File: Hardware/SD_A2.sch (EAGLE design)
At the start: 24 parts, among them IC1 74HCT245N, IC2 LM317, IC3 2716

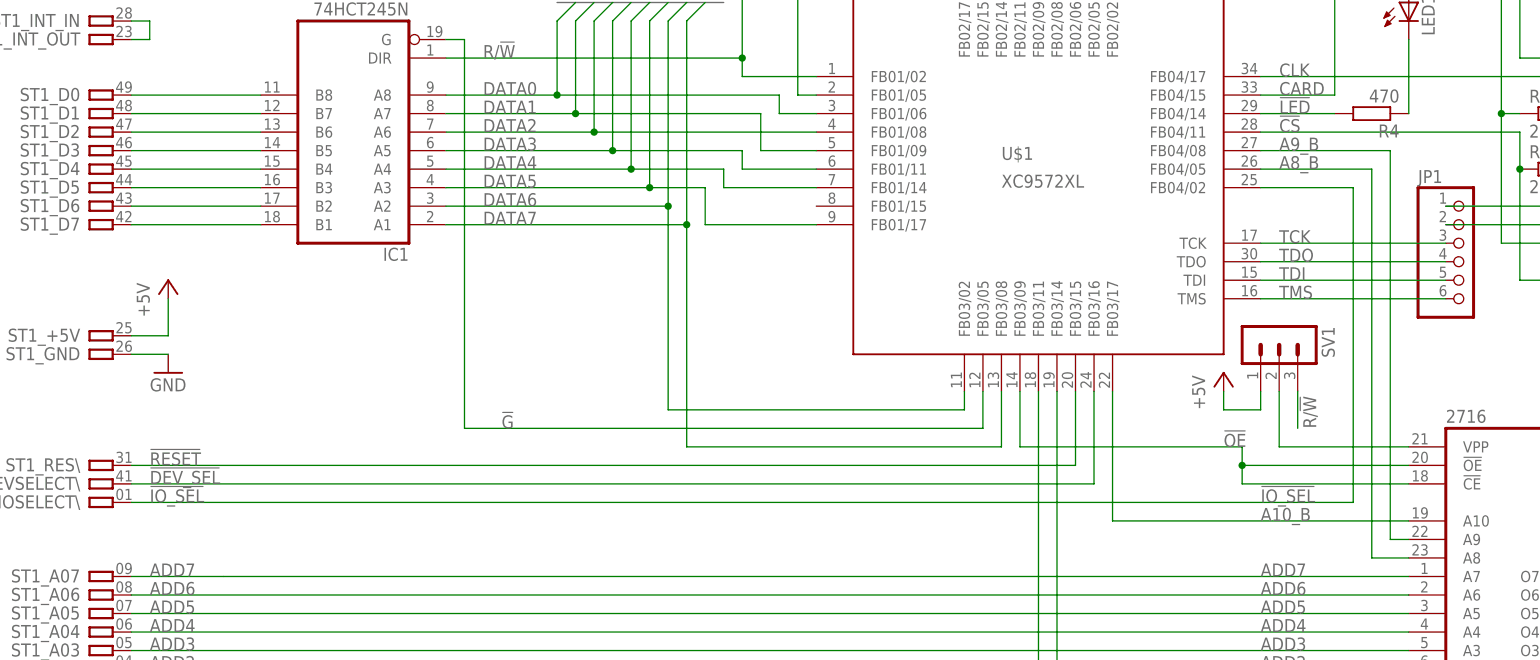
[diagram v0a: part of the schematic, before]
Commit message: Pinning changed
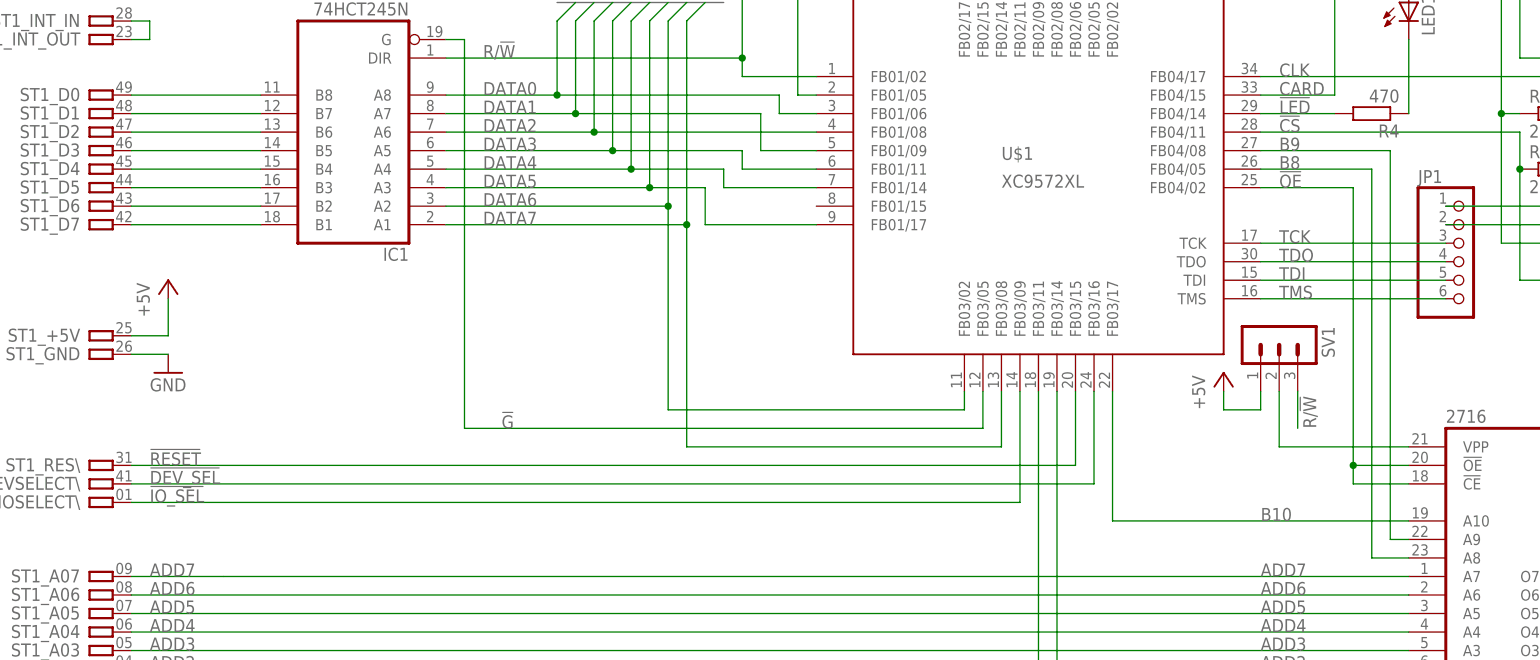
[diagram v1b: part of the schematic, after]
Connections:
- net A10_B renamed B10
- net A8_B renamed B8
- net A9_B renamed B9
- net !IO_SEL: now also U$1G$1.FB03/09; no longer U$1G$1.FB04/02
- net !OE: now also U$1G$1.FB04/02; no longer U$1G$1.FB03/09
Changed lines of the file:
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@@
 </segment>
 </net>
-<net name="A10_B" class="0">
+<net name="B10" class="0">
 <segment>
 <pinref part="IC3" gate="A" pin="A10"/>
@@
 </segment>
 </net>
-<net name="A9_B" class="0">
+<net name="B9" class="0">
 <segment>
 <pinref part="IC3" gate="A" pin="A9"/>
@@
 </segment>
 </net>
-<net name="A8_B" class="0">
+<net name="B8" class="0">
 <segment>
 <pinref part="IC3" gate="A" pin="A8"/>
@@
 <pinref part="U$1" gate="G$1" pin="FB04/05"/>
 <wire x1="246.38" y1="124.46" x2="231.14" y2="124.46" width="0.1524" layer="91"/>
-</segment>
-</net>
-<net name="!OE" class="0">
-<segment>
-<pinref part="U$1" gate="G$1" pin="FB03/09"/>
-<wire x1="198.12" y1="93.98" x2="198.12" y2="86.36" width="0.1524" layer="91"/>
-<wire x1="198.12" y1="86.36" x2="228.6" y2="86.36" width="0.1524" layer="91"/>
-<pinref part="IC3" gate="A" pin="!OE"/>
-<wire x1="251.46" y1="83.82" x2="228.6" y2="83.82" width="0.1524" layer="91"/>
-<wire x1="228.6" y1="83.82" x2="228.6" y2="86.36" width="0.1524" layer="91"/>
-<label x="226.06" y="86.36" size="1.778" layer="95"/>
-<pinref part="IC3" gate="A" pin="!CE"/>
-<wire x1="251.46" y1="81.28" x2="228.6" y2="81.28" width="0.1524" layer="91"/>
-<wire x1="228.6" y1="81.28" x2="228.6" y2="83.82" width="0.1524" layer="91"/>
-<junction x="228.6" y="83.82"/>
 </segment>
 </net>
@@
 </segment>
 </net>
-<net name="!IO_SEL" class="0">
-<segment>
-<label x="231.14" y="78.74" size="1.778" layer="95"/>
-<pinref part="U$1" gate="G$1" pin="FB04/02"/>
-<wire x1="231.14" y1="121.92" x2="243.84" y2="121.92" width="0.1524" layer="91"/>
-<wire x1="243.84" y1="121.92" x2="243.84" y2="78.74" width="0.1524" layer="91"/>
-<pinref part="ST1" gate="_IOSELECT\" pin="P"/>
-<wire x1="243.84" y1="78.74" x2="76.2" y2="78.74" width="0.1524" layer="91"/>
-<label x="78.74" y="78.74" size="1.778" layer="95"/>
-</segment>
-</net>
 <net name="!DEV_SEL" class="0">
 <segment>
@@
 </segment>
 </net>
+<net name="!OE" class="0">
+<segment>
+<label x="233.68" y="121.92" size="1.778" layer="95"/>
+<pinref part="U$1" gate="G$1" pin="FB04/02"/>
+<wire x1="231.14" y1="121.92" x2="243.84" y2="121.92" width="0.1524" layer="91"/>
+<pinref part="IC3" gate="A" pin="!OE"/>
+<wire x1="251.46" y1="83.82" x2="243.84" y2="83.82" width="0.1524" layer="91"/>
+<pinref part="IC3" gate="A" pin="!CE"/>
+<wire x1="251.46" y1="81.28" x2="243.84" y2="81.28" width="0.1524" layer="91"/>
+<wire x1="243.84" y1="81.28" x2="243.84" y2="83.82" width="0.1524" layer="91"/>
+<wire x1="243.84" y1="121.92" x2="243.84" y2="83.82" width="0.1524" layer="91"/>
+<junction x="243.84" y="83.82"/>
+</segment>
+</net>
+<net name="!IO_SEL" class="0">
+<segment>
+<pinref part="U$1" gate="G$1" pin="FB03/09"/>
+<wire x1="198.12" y1="93.98" x2="198.12" y2="78.74" width="0.1524" layer="91"/>
+<pinref part="ST1" gate="_IOSELECT\" pin="P"/>
+<wire x1="198.12" y1="78.74" x2="76.2" y2="78.74" width="0.1524" layer="91"/>
+<label x="78.74" y="78.74" size="1.778" layer="95"/>
+</segment>
+</net>

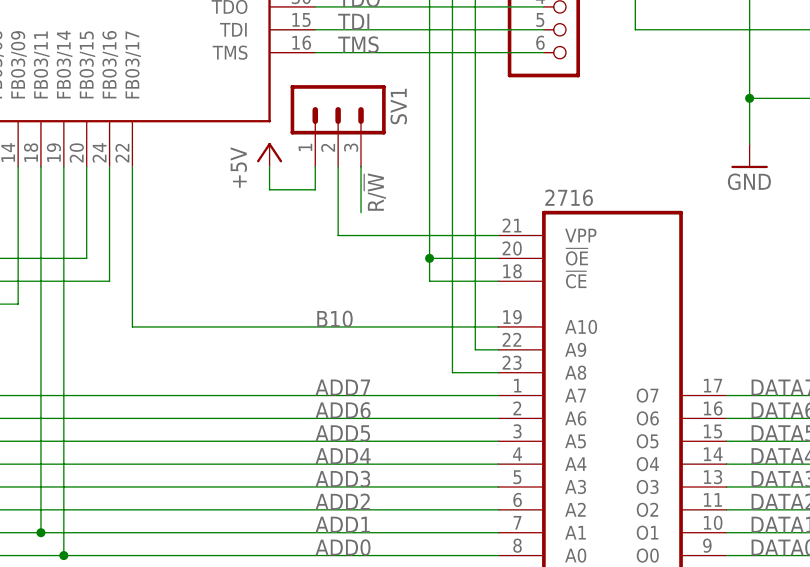
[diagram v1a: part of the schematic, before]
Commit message: !CE on GND
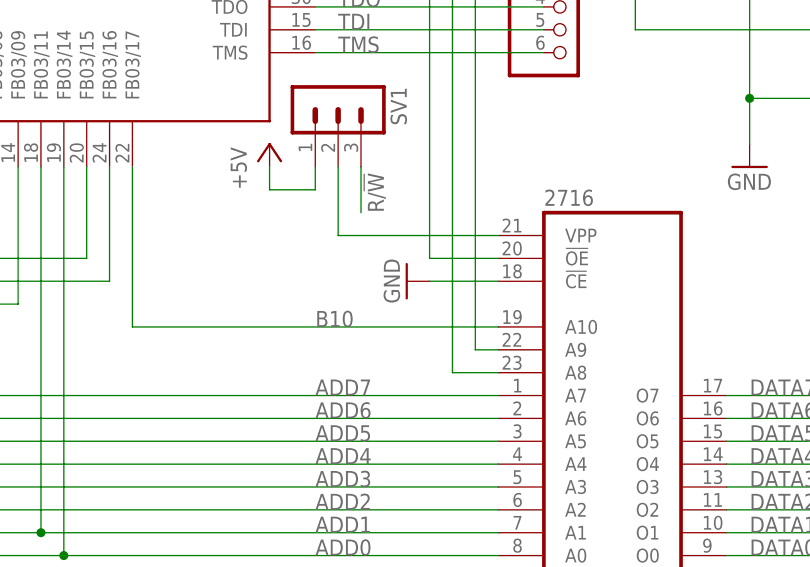
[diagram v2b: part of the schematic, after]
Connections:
- net !OE: no longer IC3A.!CE
- net GND: now also IC3A.!CE
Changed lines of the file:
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@@
 <part name="R10" library="rcl" library_urn="urn:adsk.eagle:library:334" deviceset="R-EU_" device="0204/7" value="10k"/>
 <part name="P+6" library="supply1" library_urn="urn:adsk.eagle:library:371" deviceset="+5V" device=""/>
+<part name="GND4" library="supply1" library_urn="urn:adsk.eagle:library:371" deviceset="GND" device=""/>
 </parts>
 <sheets>
@@
 <instance part="R10" gate="G$1" x="172.72" y="154.94"/>
 <instance part="P+6" gate="1" x="182.88" y="160.02"/>
+<instance part="GND4" gate="1" x="241.3" y="81.28" rot="R270"/>
 </instances>
 <busses>
@@
 <wire x1="256.54" y1="116.84" x2="279.4" y2="116.84" width="0.1524" layer="91"/>
 <junction x="279.4" y="116.84"/>
+</segment>
+<segment>
+<pinref part="IC3" gate="A" pin="!CE"/>
+<pinref part="GND4" gate="1" pin="GND"/>
+<wire x1="251.46" y1="81.28" x2="243.84" y2="81.28" width="0.1524" layer="91"/>
 </segment>
 </net>
@@
 <pinref part="IC3" gate="A" pin="!OE"/>
 <wire x1="251.46" y1="83.82" x2="243.84" y2="83.82" width="0.1524" layer="91"/>
-<pinref part="IC3" gate="A" pin="!CE"/>
-<wire x1="251.46" y1="81.28" x2="243.84" y2="81.28" width="0.1524" layer="91"/>
-<wire x1="243.84" y1="81.28" x2="243.84" y2="83.82" width="0.1524" layer="91"/>
 <wire x1="243.84" y1="121.92" x2="243.84" y2="83.82" width="0.1524" layer="91"/>
-<junction x="243.84" y="83.82"/>
-</segment>
-</net>
+</segment>
+</net>

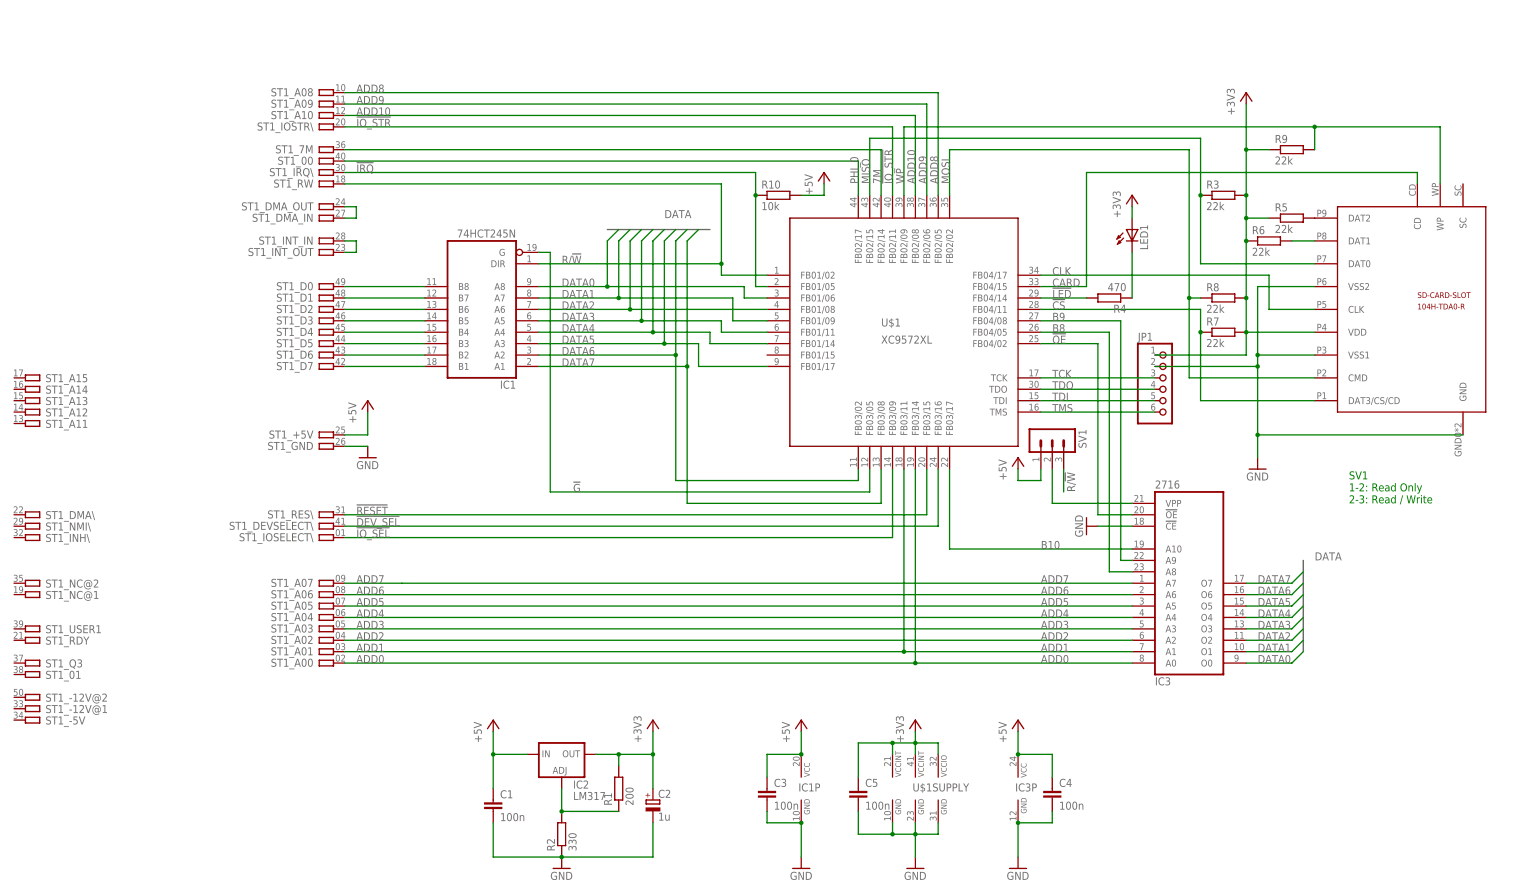
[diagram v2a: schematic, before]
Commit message: Pin changes, libraries added
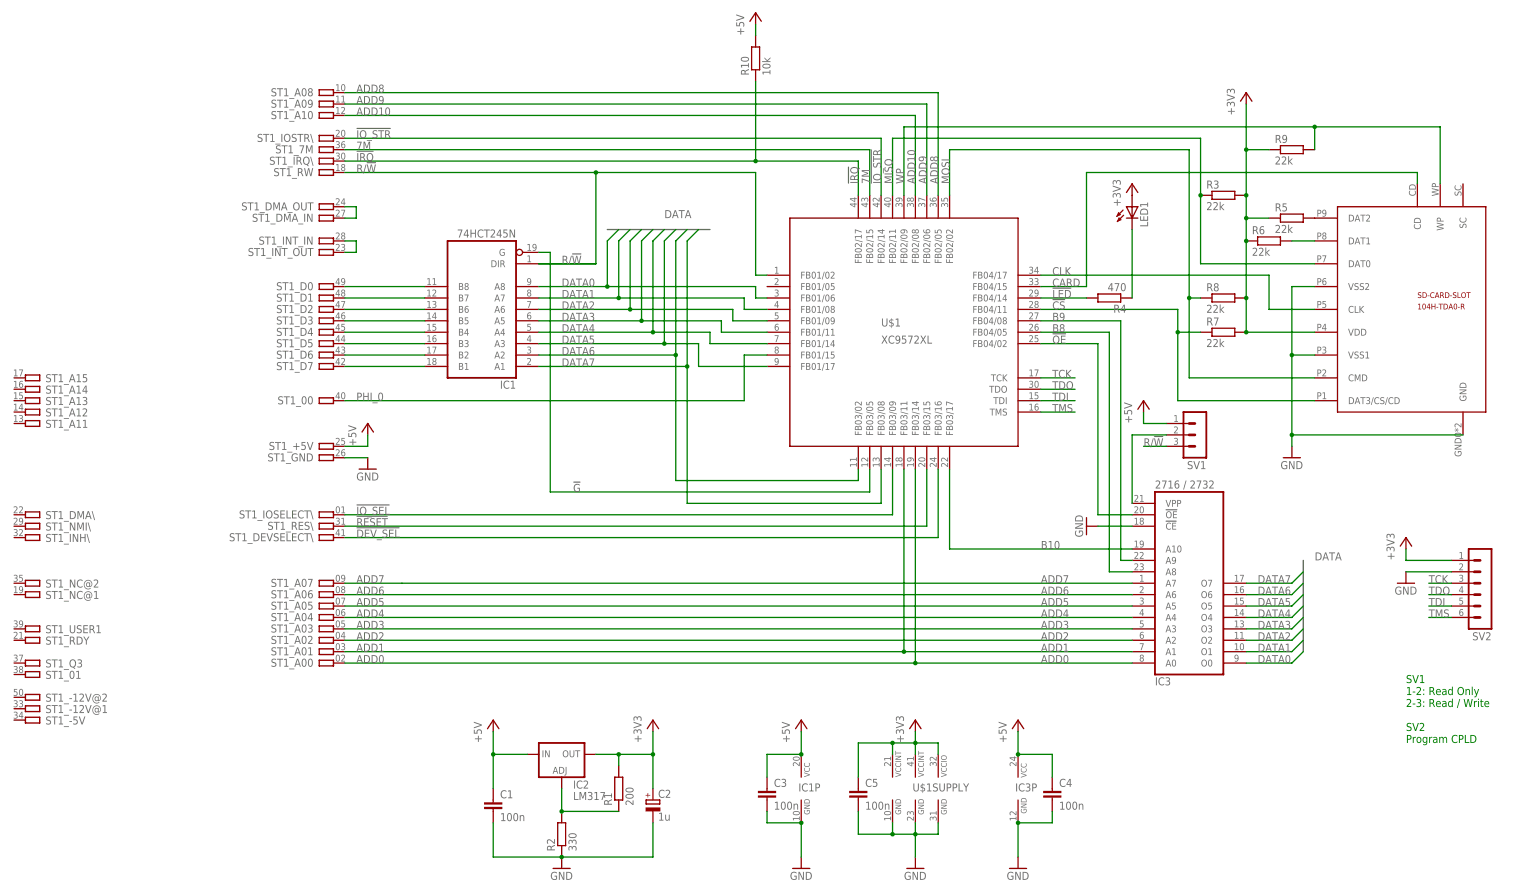
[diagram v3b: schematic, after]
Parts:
- removed JP1: (no value), pinhead:PINHD-1X6
- added SV2: (no value), con-lstb:MA06-1
- IC3: value 2716 -> 2716 / 2732
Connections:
- net !IO_STR: now also U$1G$1.FB02/14; no longer U$1G$1.FB02/11
- net !IRQ: now also U$1G$1.FB02/17; no longer U$1G$1.FB01/05
- net +3V3: now also SV2.1; no longer JP1.1
- net 7M: now also U$1G$1.FB02/15; no longer U$1G$1.FB02/14
- net DATA1: now also U$1G$1.FB01/08; no longer U$1G$1.FB01/09
- net DATA2: now also U$1G$1.FB01/09; no longer U$1G$1.FB01/08
- net GND: now also SV2.2; no longer JP1.2
- net MISO: now also U$1G$1.FB02/11; no longer U$1G$1.FB02/15
- net PHI_0: now also U$1G$1.FB01/15; no longer U$1G$1.FB02/17
- net TCK: now also SV2.3; no longer JP1.3
- net TDI: now also SV2.5; no longer JP1.5
- net TDO: now also SV2.4; no longer JP1.4
- net TMS: now also SV2.6; no longer JP1.6
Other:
- note added: "SV1 1-2: Read Only 2-3: Read / Write SV2 Program CPLD"
- note removed: "SV1 1-2: Read Only 2-3: Read / Write"
- moved on the sheet: LED1, R10, ST1_+5V, ST1_00, ST1_DEVSELECT\, ST1_GND, ST1_IOSELECT\, ST1_IOSTR\, ST1_IRQ\, ST1_RES\, ST1_RW, SV1

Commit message: R and C changed to SMD
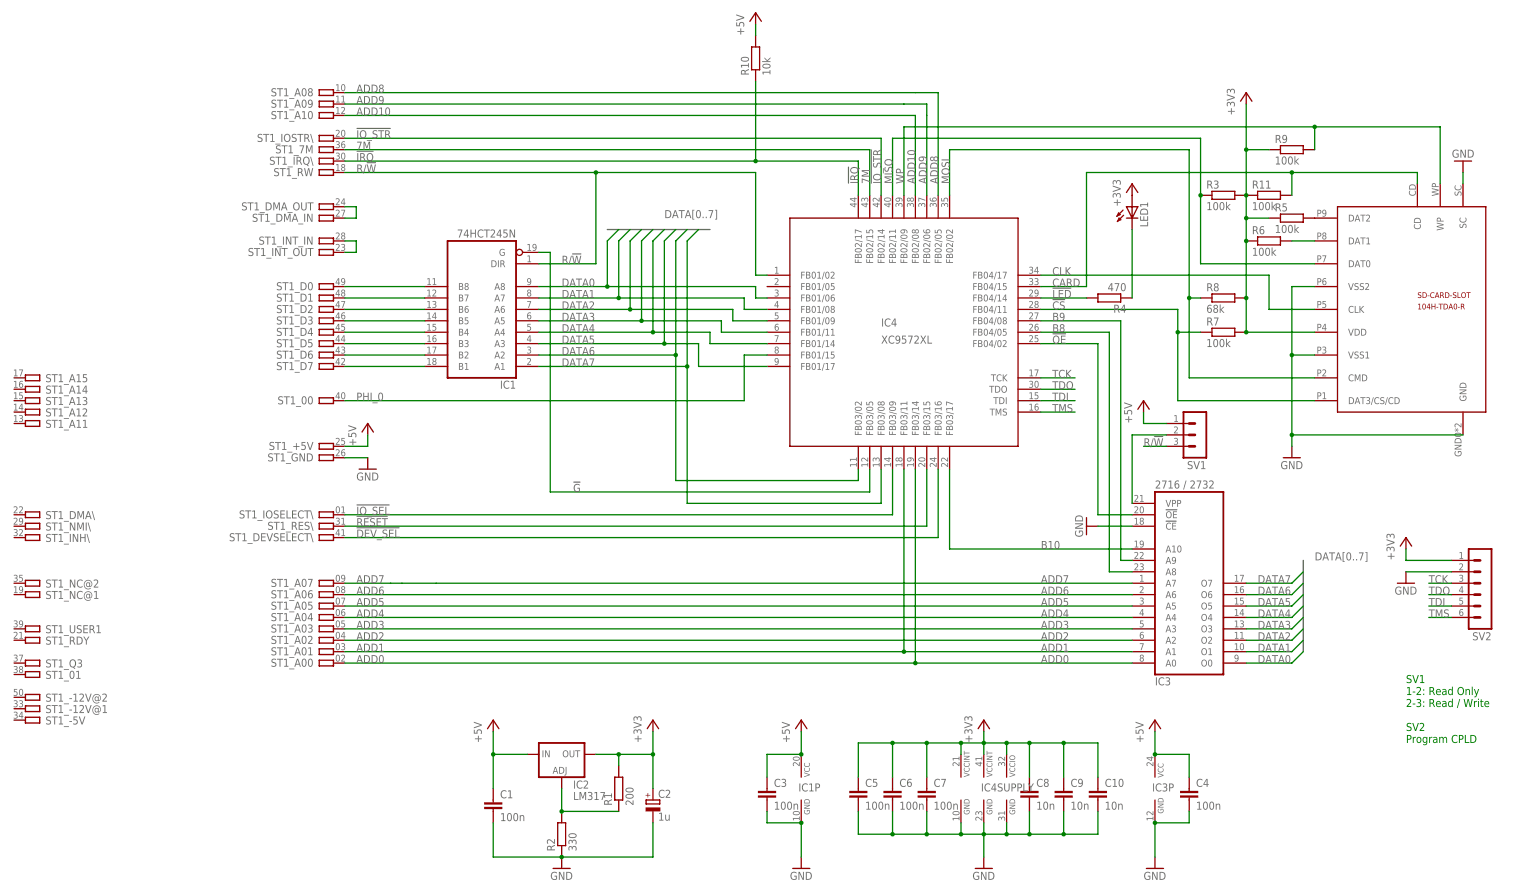
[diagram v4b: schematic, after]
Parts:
- added C10, C8, C9: 10n, rcl:C-EUC0603K
- added C6, C7: 100n, rcl:C-EUC0603K
- added R11: 100k, rcl:R-EU_R0603
- C1, C3, C4, C5: device rcl:C-EU025-025X050 -> rcl:C-EUC0603K
- R1, R10, R2, R4: device rcl:R-EU_0204/7 -> rcl:R-EU_R0603
- R3, R5, R6, R7, R9: value 22k -> 100k; device rcl:R-EU_0204/7 -> rcl:R-EU_R0603
- R8: value 22k -> 68k; device rcl:R-EU_0204/7 -> rcl:R-EU_R0603
- renumbered U$1 to IC4
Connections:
- net +3V3: now also C10.1, C6.1, C7.1, C8.1, C9.1, R11.1
- net CARD: now also R11.2
- net GND: now also C10.2, C6.2, C7.2, C8.2, C9.2, U$2.SC
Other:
- moved on the sheet: C4, IC3P

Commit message: Small changes on board
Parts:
- C2: device rcl:CPOL-EUE2.5-5 -> rcl:CPOL-EU153CLV-0405
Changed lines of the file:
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@@
 <?xml version="1.0" encoding="utf-8"?>
 <!DOCTYPE eagle SYSTEM "eagle.dtd">
-<eagle version="7.7.0">
+<eagle version="8.2.2">
 <drawing>
 <settings>
@@
 <part name="IC1" library="74xx-eu" deviceset="74*245" device="N" technology="HCT"/>
 <part name="IC2" library="v-reg" deviceset="LM317TL" device="" value="LM317"/>
-<part name="C2" library="rcl" deviceset="CPOL-EU" device="E2.5-5" value="1u"/>
+<part name="C2" library="rcl" library_urn="urn:adsk.eagle:library:334" deviceset="CPOL-EU" device="153CLV-0405" value="1u"/>
 <part name="R1" library="rcl" deviceset="R-EU_" device="R0603" value="200"/>
 <part name="R2" library="rcl" deviceset="R-EU_" device="R0603" value="330"/>
@@
 which will not be processed correctly with this version.
 </note>
+<note version="8.2" severity="warning">
+Since Version 8.2, Eagle supports online libraries. The ids
+of those online libraries will not be understood (or retained)
+with this version.
+</note>
 </compatibility>
